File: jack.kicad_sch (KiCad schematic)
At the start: 18 parts, among them J1 35RASMT5CHNTRX, J3 35RASMT5CHNTRX, Q1 Q_NPN_BCE, Q2 Q_PMOS_DGS, Q3 Q_PMOS_DGS, U4 74LVC1G17, U5 74LVC1G17, U6 74LVC1G17, U7 74LVC1G17

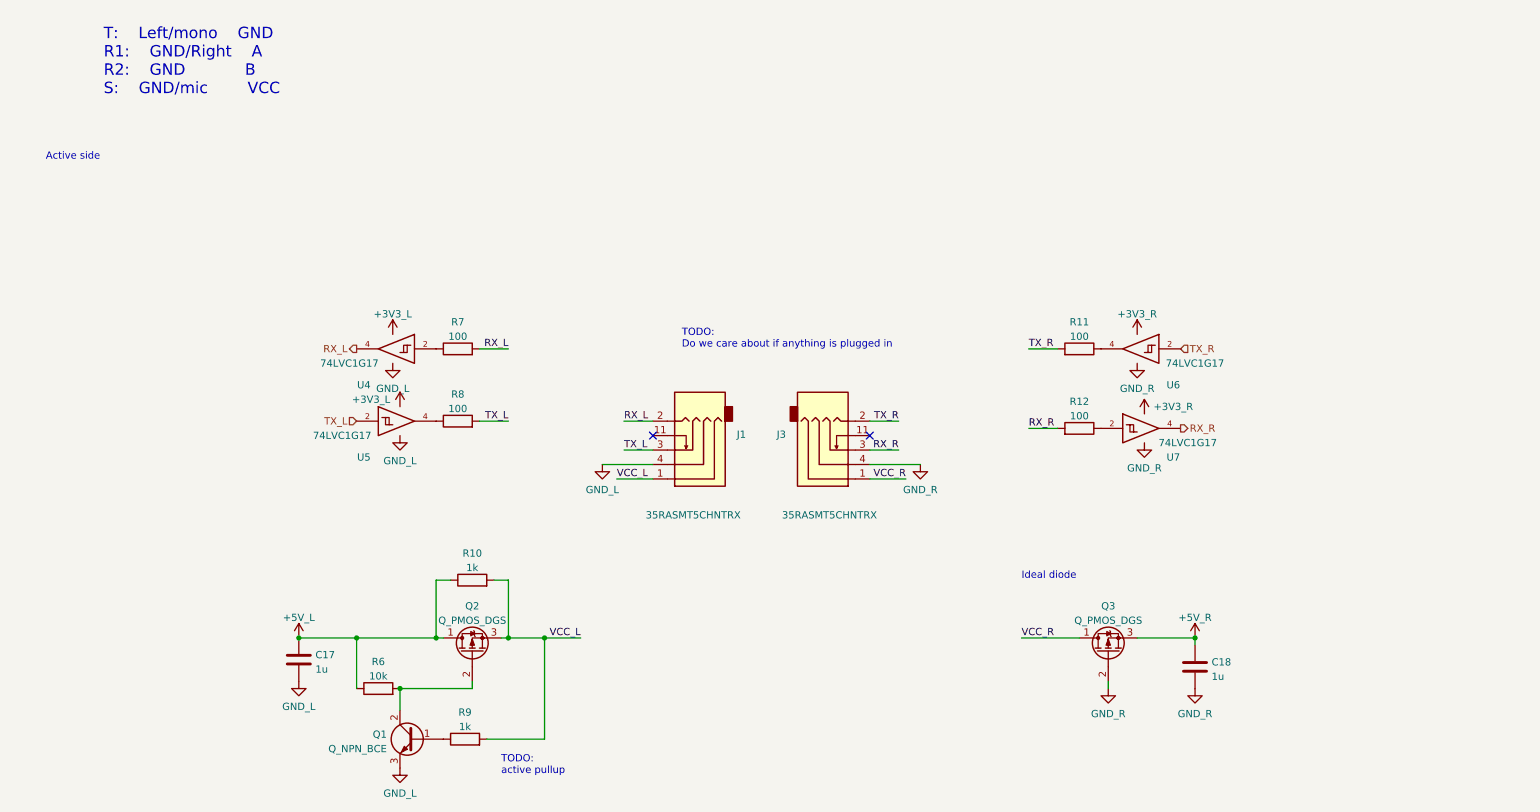
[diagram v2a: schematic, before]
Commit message: Add second micro back in, and added some footprints
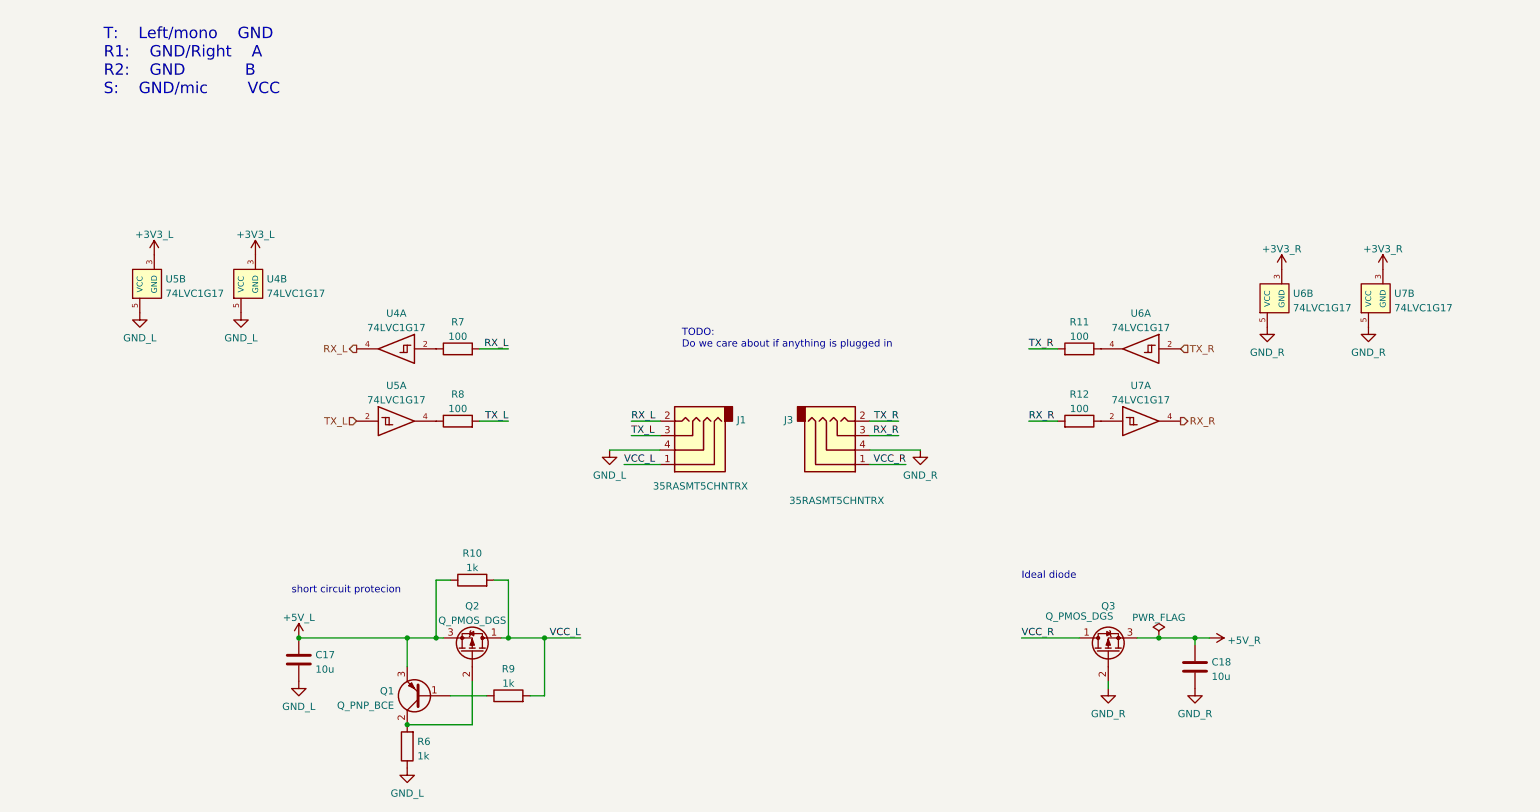
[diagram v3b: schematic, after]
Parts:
- removed Q1: Q_NPN_BCE, symbol Device:Q_NPN_BCE
- removed U4, U5, U6, U7: 74LVC1G17, symbol 74xGxx:74LVC1G17
- added Q1: Q_PNP_BCE, symbol Device:Q_PNP_BCE
- added U4, U5, U6, U7: 74LVC1G17, Package_TO_SOT_SMD:SOT-23-5, symbol arisu-split:74LVC1G17
- C17, C18: value 1u -> 10u; footprint (none) -> Capacitor_SMD:C_0805_2012Metric
- J1, J3: footprint (none) -> arisu-split:35RASMT5CHNTRX
- R10, R11, R12, R7, R8, R9: footprint (none) -> Capacitor_SMD:C_0402_1005Metric
- R6: value 10k -> 1k; footprint (none) -> Capacitor_SMD:C_0402_1005Metric
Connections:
- net +3V3_L: now also U4.3 (GND), U5.3 (GND)
- net +5V_L: now also Q2.3 (S), Q1.3 (E); no longer Q2.1 (D), R6.1
- net RX_L: now also U4.4
- net RX_R: now also U7.4
- net TX_L: now also U5.2
- net TX_R: now also U6.2
- net VCC_L: now also Q2.1 (D); no longer Q2.3 (S)
- net at R9.1: now also Q1.1 (B)
- net at Q2.2 (G), R6.2: now also Q1.2 (C)
- net at R11.1: now also U6.4
- net at R7.1: now also U4.2
- net at R8.1: now also U5.4
- net at R12.1: now also U7.2
- net GND renamed GND_R
- net GND_R: now also U6.5 (VCC), U7.5 (VCC); no longer C17.2, J1.4
- new net +3V3_R: U6.3 (GND), U7.3 (GND)
- new net GND_L: C17.2, J1.4, R6.1, U4.5 (VCC), U5.5 (VCC)
- no-connect marks 2 -> 0
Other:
- note added: "short circuit protecion"
- note removed: "Active side"
- note removed: "TODO: active pullup"
- moved on the sheet: Q2, R12, R9

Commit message: Schematic mostly finished
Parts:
- removed Q1: Q_PNP_BCE, symbol Device:Q_PNP_BCE
- removed Q2, Q3: Q_PMOS_DGS, symbol Device:Q_PMOS_DGS
- added Q1: BC807, Package_TO_SOT_SMD:SOT-23, symbol Transistor_BJT:BC807
- added Q2, Q3: DMG2301L, Package_TO_SOT_SMD:SOT-23, symbol Transistor_FET:DMG2301L
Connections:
- net +3V3_L: now also U4.5 (VCC), U5.5 (VCC); no longer U4.3 (GND), U5.3 (GND)
- net +3V3_R: now also U6.5 (VCC), U7.5 (VCC); no longer U6.3 (GND), U7.3 (GND)
- net +5R: now also Q3.2 (S)
- net +5V_L: now also Q1.2 (E), Q2.3 (D)
- net GND_L: now also U4.3 (GND), U5.3 (GND); no longer U4.5 (VCC), U5.5 (VCC)
- net GND_R: now also U6.3 (GND), U7.3 (GND), Q3.1 (G); no longer U6.5 (VCC), U7.5 (VCC)
- net VCC_L: now also Q2.2 (S)
- net VCC_R: now also Q3.3 (D)
- net at R6.2: now also Q1.3 (C), Q2.1 (G)
- net at R9.1: now also Q1.1 (B)

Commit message: more layout, and some 3d files
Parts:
- removed C18: 10u, Capacitor_SMD:C_0805_2012Metric, symbol Device:C
- added C37, C38, C39, C40: 100n, Capacitor_SMD:C_0603_1608Metric, symbol Device:C
- R10, R11, R12, R6, R7, R8, R9: footprint Capacitor_SMD:C_0402_1005Metric -> Capacitor_SMD:C_0603_1608Metric
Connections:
- net +3V3_L: now also C37.1, C38.1
- net +3V3_R: now also C39.1, C40.1
- net +5V_L: now also Q2.2 (S); no longer Q2.3 (D)
- net GND_L: now also C37.2, C38.2
- net GND_R: now also C39.2, C40.2
- net RX_L: no longer J1.2, R7.2
- net RX_R: no longer J3.3, R12.2
- net TX_L: no longer J1.3, R8.2
- net TX_R: no longer J3.2, R11.2
- net VCC_L: now also Q2.3 (D); no longer Q2.2 (S)
- new net C_RX_L: J1.2, R7.2
- new net C_RX_R: J3.3, R12.2
- new net C_TX_L: J1.3, R8.2
- new net C_TX_R: J3.2, R11.2
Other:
- moved on the sheet: Q2, U4B, U7B

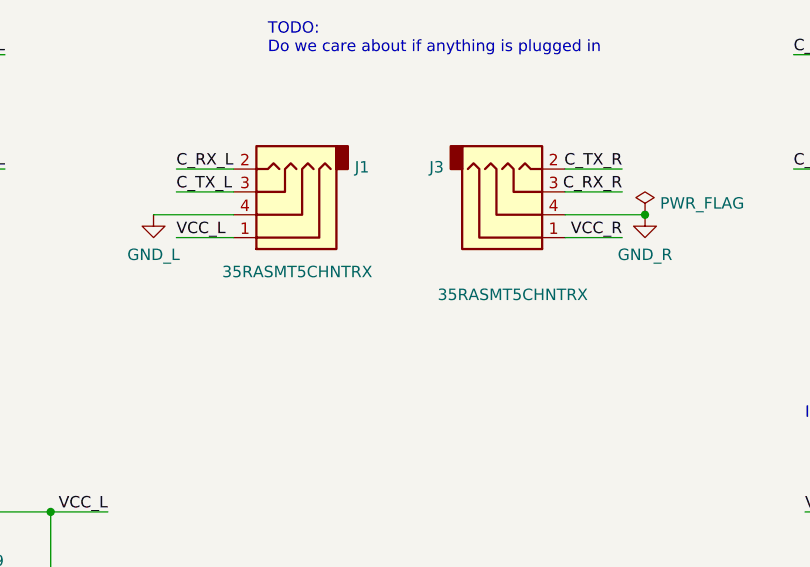
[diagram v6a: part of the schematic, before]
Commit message: Finished layout (for now), board outline, and new trrs jacks
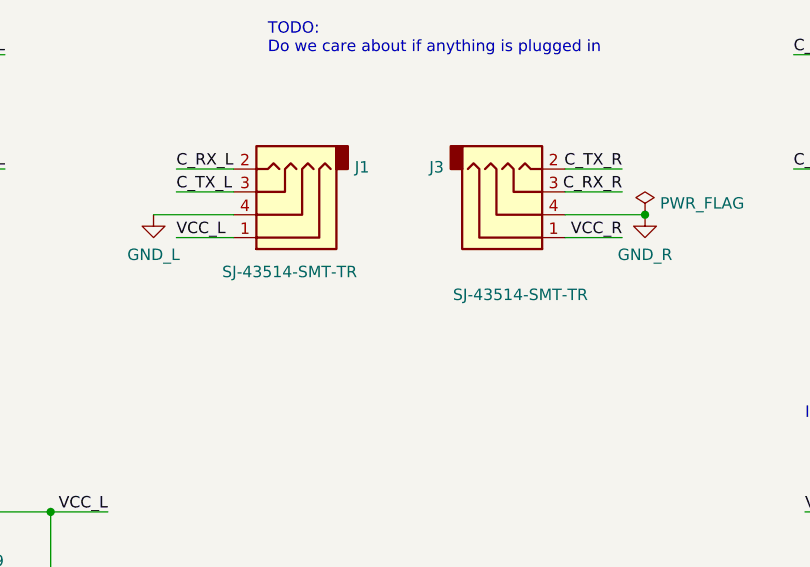
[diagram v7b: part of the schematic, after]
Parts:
- J1, J3: value 35RASMT5CHNTRX -> SJ-43514-SMT-TR; footprint arisu-split:35RASMT5CHNTRX -> arisu-split:SJ-43514-SMT-TR; symbol arisu-split:35RASMT5CHNTRX -> arisu-split:SJ-43514-SMT-TR
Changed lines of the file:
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@@
     (pin "5")
   )
-  (symbol (lib_id "arisu-split:35RASMT5CHNTRX") (at 127 93.98 180) (unit 1)
+  (symbol (lib_id "arisu-split:SJ-43514-SMT-TR") (at 127 93.98 180) (unit 1)
     (in_bom yes) (on_board yes)
     (property "Reference" "J1" (id 0) (at 136.652 91.2403 0)
       (effects (font (size 1.27 1.27)) (justify right))
     )
-    (property "Value" "35RASMT5CHNTRX" (id 1) (at 121.92 102.87 0)
-      (effects (font (size 1.27 1.27)) (justify right))
-    )
-    (property "Footprint" "arisu-split:35RASMT5CHNTRX" (id 2) (at 128.27 93.98 0)
+    (property "Value" "SJ-43514-SMT-TR" (id 1) (at 121.92 102.87 0)
+      (effects (font (size 1.27 1.27)) (justify right))
+    )
+    (property "Footprint" "arisu-split:SJ-43514-SMT-TR" (id 2) (at 128.27 93.98 0)
       (effects (font (size 1.27 1.27)) hide)
     )
@@
     (pin "1")
   )
-  (symbol (lib_id "arisu-split:35RASMT5CHNTRX") (at 156.21 93.98 0) (mirror x) (unit 1)
+  (symbol (lib_id "arisu-split:SJ-43514-SMT-TR") (at 156.21 93.98 0) (mirror x) (unit 1)
     (in_bom yes) (on_board yes)
     (property "Reference" "J3" (id 0) (at 146.558 91.2403 0)
       (effects (font (size 1.27 1.27)) (justify right))
     )
-    (property "Value" "35RASMT5CHNTRX" (id 1) (at 162.56 105.41 0)
-      (effects (font (size 1.27 1.27)) (justify right))
-    )
-    (property "Footprint" "arisu-split:35RASMT5CHNTRX" (id 2) (at 154.94 93.98 0)
-      (effects (font (size 1.27 1.27)) hide)
-    )
+    (property "Value" "SJ-43514-SMT-TR" (id 1) (at 162.56 105.41 0)
+      (effects (font (size 1.27 1.27)) (justify right))
+    )
+    (property "Footprint" "arisu-split:SJ-43514-SMT-TR" (id 2) (at 154.94 93.98 0)
+      (effects (font (size 1.27 1.27)) hide)
+    )

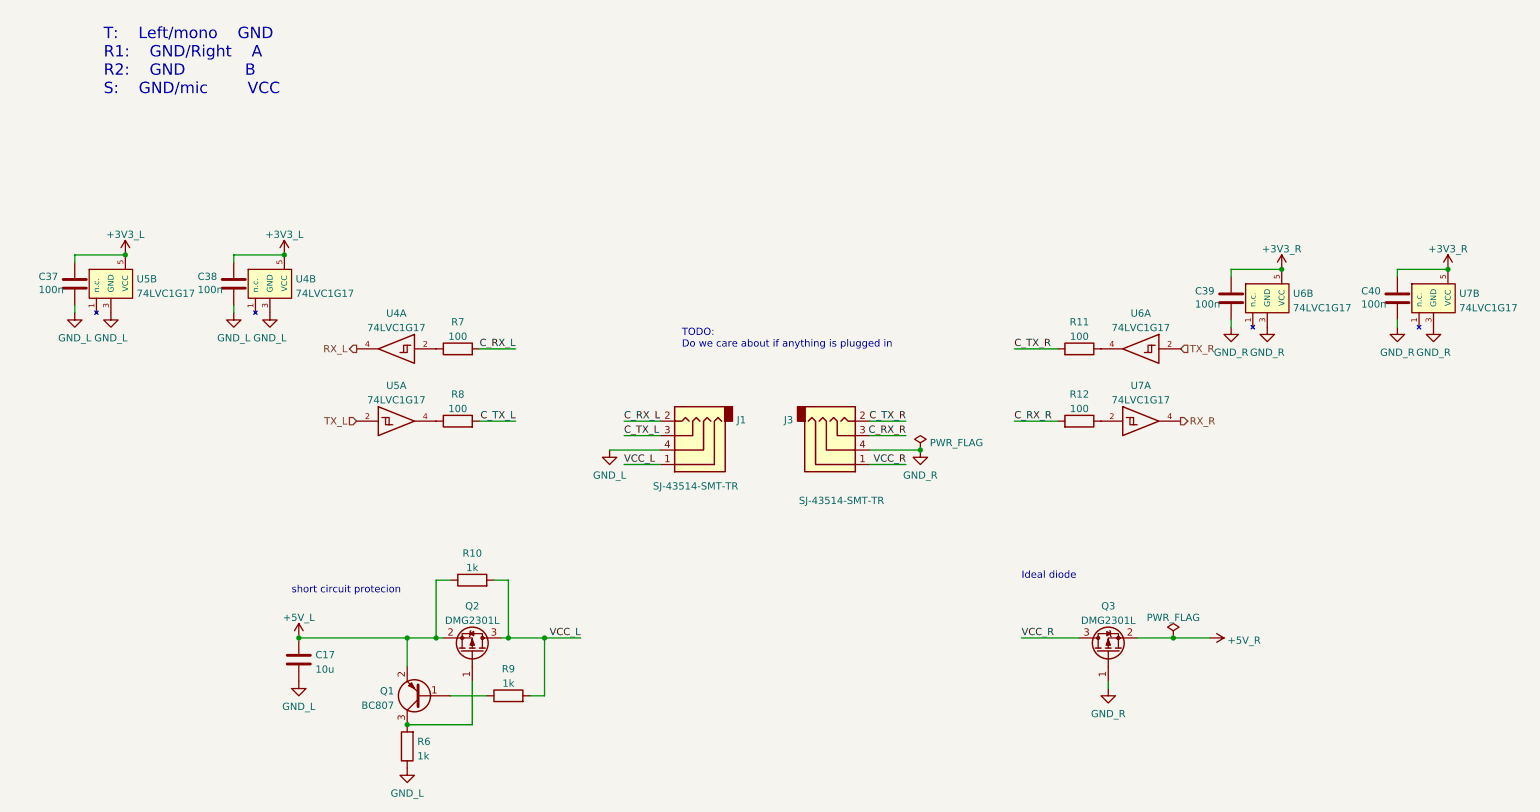
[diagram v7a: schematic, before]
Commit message: replace usb right side, rotate micro, add protection diodes, trrs protection circuit mirrored, run pin cap removved, resistor footprints replaced
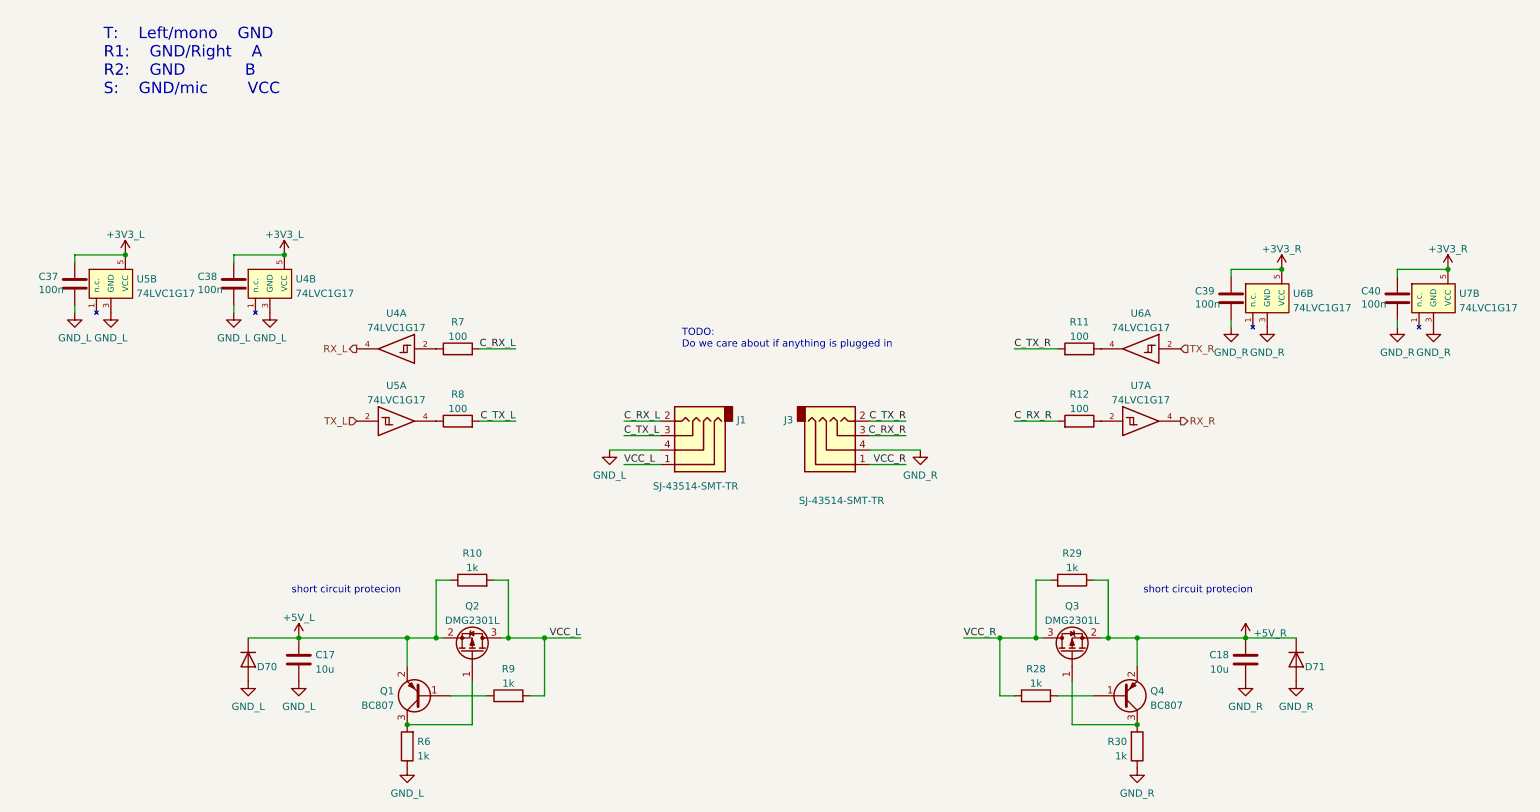
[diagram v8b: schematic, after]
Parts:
- added C18: 10u, Capacitor_SMD:C_0805_2012Metric, symbol Device:C
- added D70, D71: ~, Diode_SMD:D_SOD-123, symbol Device:D
- added Q4: BC807, Package_TO_SOT_SMD:SOT-23, symbol Transistor_BJT:BC807
- added R28, R29, R30: 1k, Resistor_SMD:R_0603_1608Metric, symbol Device:R
- R10, R11, R12, R6, R7, R8, R9: footprint Capacitor_SMD:C_0603_1608Metric -> Resistor_SMD:R_0603_1608Metric
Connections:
- net +5R: now also C18.1, D71.1 (K), Q4.2 (E), R29.1
- net +5V_L: now also D70.1 (K)
- net GND_L: now also D70.2 (A)
- net GND_R: now also C18.2, D71.2 (A), R30.1; no longer Q3.1 (G)
- net VCC_R: now also R28.2, R29.2
- new net: Q4.1 (B), R28.1
- new net: Q3.1 (G), Q4.3 (C), R30.2
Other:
- note removed: "Ideal diode"
